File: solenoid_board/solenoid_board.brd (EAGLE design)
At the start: 30.1 x 30.1 mm, 19 parts, among them Q1 MOSFET-NCHANNELSMD, Q2 MOSFET-NCHANNELSMD, Q3 MOSFET-NCHANNELSMD, Q4 MOSFET-NCHANNELSMD

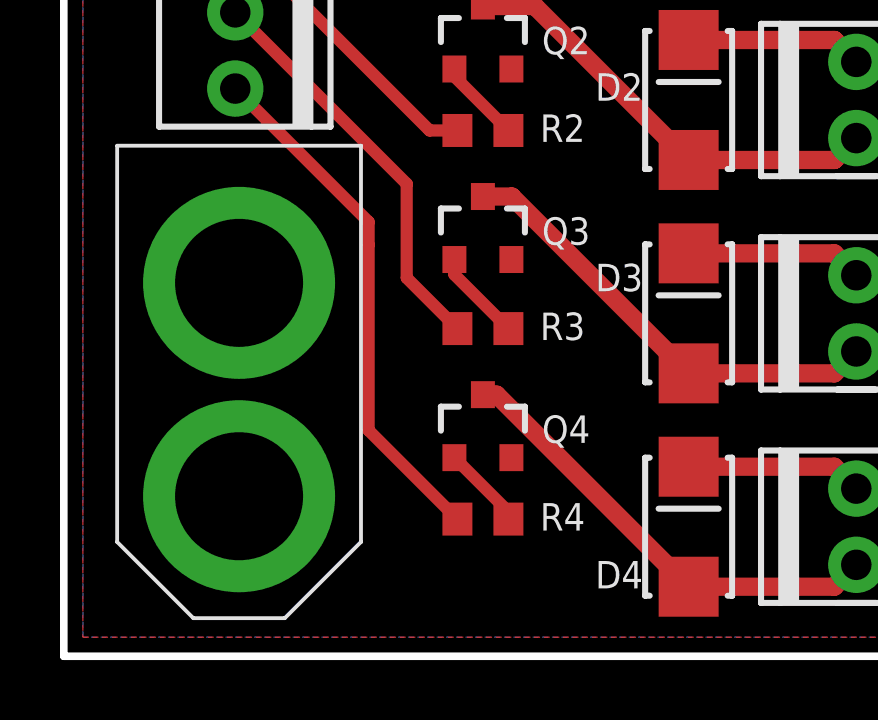
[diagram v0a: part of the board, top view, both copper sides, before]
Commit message: Fixed XT60 connector in pie.lbr. Changed battery connector on sherlock to have 4 pins instead of 5. Replaced XT60 on sherlock, solenoid board, and grizzly bear with new version.
Change-Id: Ic4b688068eb477e37db8d2c4f2efb7678e25c5b6
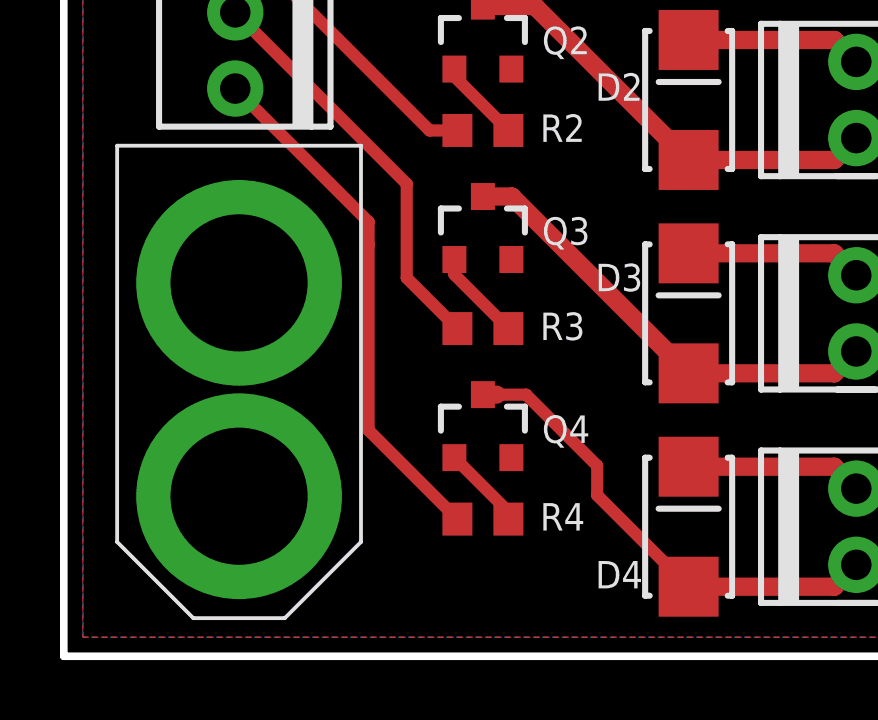
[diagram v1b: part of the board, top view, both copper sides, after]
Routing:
- net N$3: track 15.4 -> 16.0 mm
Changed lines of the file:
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@@
 <?xml version="1.0" encoding="utf-8"?>
 <!DOCTYPE eagle SYSTEM "eagle.dtd">
-<eagle version="6.2">
+<eagle version="6.3">
 <drawing>
 <settings>
@@
 </class>
 </classes>
-<designrules>
+<designrules name="advancedcircuits-33each-pie">
 <description language="de">&lt;b&gt;EAGLE Design Rules&lt;/b&gt;
 &lt;p&gt;
@@
 <param name="mtIsolate" value="9mil 40mil 9mil 0.1499mm 0.2007mm 0.1499mm 0.2007mm 0.1499mm 0.2007mm 0.1499mm 0.2007mm 0.1499mm 0.2007mm 0.1499mm 0.2007mm"/>
 <param name="mdWireWire" value="6mil"/>
-<param name="mdWirePad" value="6mil"/>
+<param name="mdWirePad" value="10mil"/>
 <param name="mdWireVia" value="6mil"/>
 <param name="mdPadPad" value="6mil"/>
@@
 <param name="mdViaViaSameLayer" value="8mil"/>
 <param name="mnLayersViaInSmd" value="2"/>
-<param name="mdCopperDimension" value="10mil"/>
+<param name="mdCopperDimension" value="25mil"/>
 <param name="mdDrill" value="7mil"/>
 <param name="mdSmdStop" value="0mil"/>
@@
 <wire x1="25.686" y1="2.318" x2="26.416" y2="3.048" width="0.6096" layer="1"/>
 <wire x1="13.97" y1="8.72" x2="14.426" y2="8.72" width="0.6096" layer="1"/>
-<wire x1="14.426" y1="8.72" x2="20.828" y2="2.318" width="0.6096" layer="1"/>
+<wire x1="14.426" y1="8.72" x2="15.41" y2="8.72" width="0.4064" layer="1"/>
+<wire x1="15.41" y1="8.72" x2="17.78" y2="6.35" width="0.4064" layer="1"/>
+<wire x1="17.78" y1="6.35" x2="17.78" y2="5.366" width="0.4064" layer="1"/>
+<wire x1="17.78" y1="5.366" x2="20.828" y2="2.318" width="0.4064" layer="1"/>
 </signal>
 <signal name="N$4" class="1">

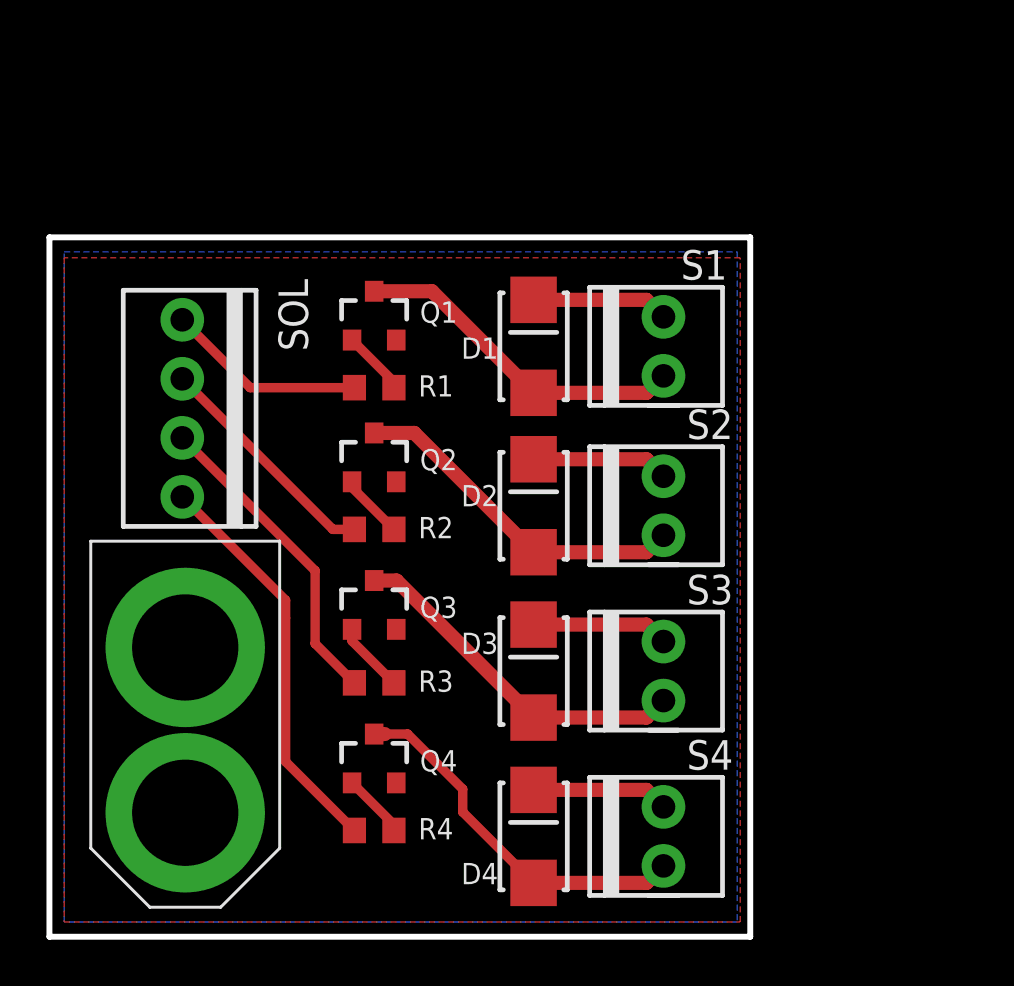
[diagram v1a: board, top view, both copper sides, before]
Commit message: Updated Solenoid Board to Rev C
- Added 10k pull-down resistors to MOSFET gates

DFM: https://www.freedfm.com/freedfm/0019486703400185/results/summary2.htm

Change-Id: I212b2e5e4622d924b76152e8610cd9dcc6a01ff7
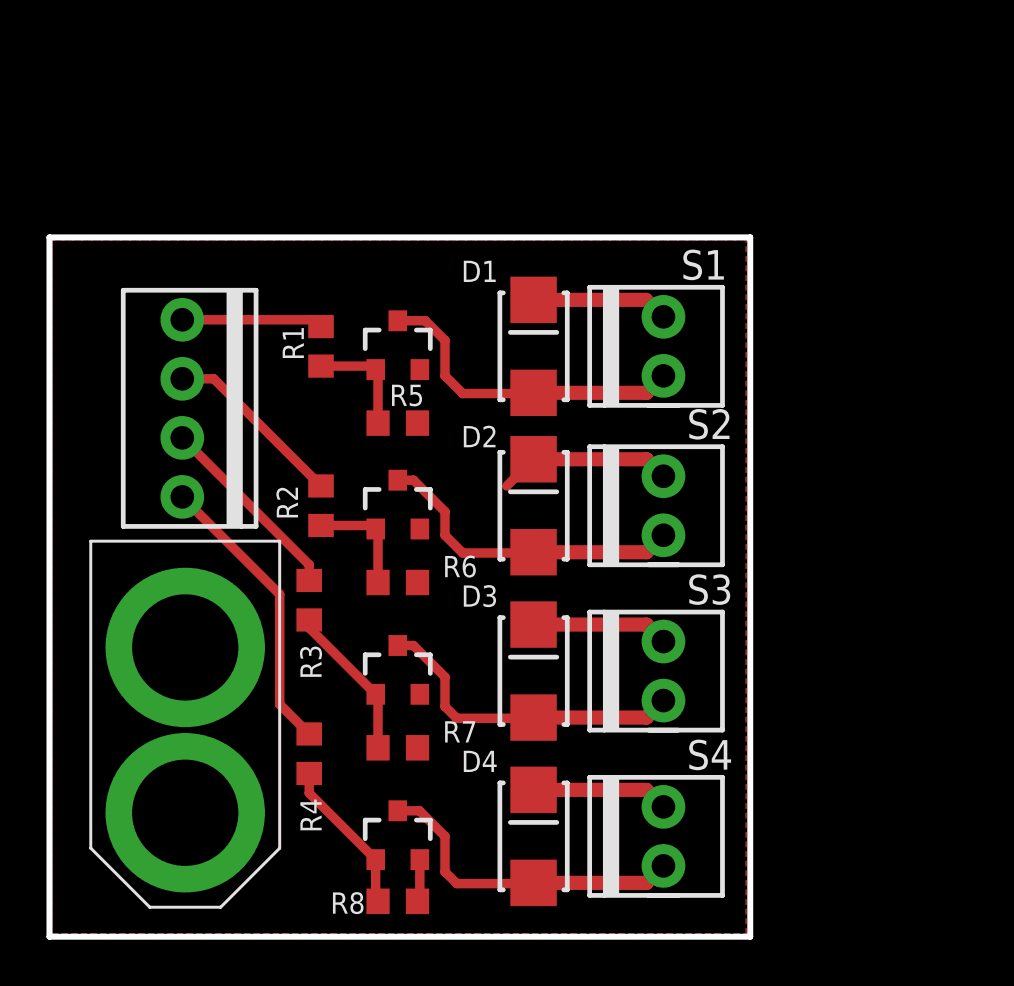
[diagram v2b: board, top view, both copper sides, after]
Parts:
- added R5, R6, R7, R8: 10k, resistor:R0603
- moved R3 4.52 mm to (11.2, 14.5), turned to 270 degrees
- moved R4 4.33 mm to (11.2, 7.87), turned to 270 degrees
- moved Q4 3.45 mm to (15.0, 4.32)
- moved Q3 2.97 mm to (15.0, 11.4)
- moved R1 2.90 mm to (11.7, 25.4), turned to 90 degrees
- moved R2 2.50 mm to (11.7, 18.5), turned to 270 degrees
- moved Q2 2.27 mm to (15.0, 18.5)
- moved Q1 1.63 mm to (15.0, 25.4)
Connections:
- net GND: now also R5.1, R6.1, R7.1, R8.1
- net N$15: now also R5.2
- net N$16: now also R6.2
- net N$17: now also R7.2
- net N$18: now also R8.2
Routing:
- net N$6: track 13.6 -> 8.40 mm
- net N$7: track 17.4 -> 12.5 mm
- net N$18: track 2.79 -> 6.78 mm
- net N$17: track 3.05 -> 6.78 mm
- net N$1: track 8.70 -> 6.09 mm
- net N$5: track 10.1 -> 7.88 mm
- net N$3: track 16.0 -> 13.9 mm
- net N$16: track 2.79 -> 4.82 mm
- net N$15: track 2.79 -> 4.82 mm
- net GND: track 0.05 -> 1.84 mm
- net 12V: track 23.6 -> 25.2 mm
- net N$4: track 15.2 -> 13.8 mm
- net N$8: track 14.9 -> 13.6 mm
- net N$2: track 14.6 -> 13.9 mm
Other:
- board text added: "2012.12.05"
- board text added: "Revision C"
- board text removed: "2012.11.19"
- board text removed: "Revision B"

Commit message: Updated Sherlock, Watson & Solenoid Board to Rev D. Updated pie.lbr.
- Put SSOP16 footprint and symbol (from Sparkfun.lbr) in pie.lbr.
  Can be used as a template for any SSOP16 device.
- Created SSOP14 footprint and symbol in pie.lbr using SSOP16.
  Can be used as a template for any SSOP14 device.
- Added QUADNOR device to pie.lbr
- Added VCC and enable pin to solenoid connector on Watson
- Added enable pin for solenoid board on Sherlock
- Added quad-NOR gate onto Solenoid Board
- Added VCC and enable pin for quad-NOR gate on Solenoid Board
- Added 0.1uF capacitors between VCC&GND and 12V&GND for Solenoid Board
- Added mounting holes to Solenoid Board
- Added additional holes to Sherlock and Watson for the testing jig
- Replaced all holes with standoff part in pie.lbr
- Gave each hole a value, either "Mounting", "Test" or "Mounting + Test"
  to state their purpose.
- Added/copied devices on boards that were NOT in pie.lbr TO pie.lbr
- Removed unnecessary packages from copied devices
- Manually set pad diameters for through-hole packages that were
  added/created/already there for these three boards
- Added PARTNUMBER attribute to the library parts added/copied/
  created/already there for these three boards
- Moved all Sherlock passives to the top

RYAN: I fixed what you asked for this revision. If this goes
through, I will then work on fixing everything else you told me to.

Sherlock DFM: https://www.freedfm.com/freedfm/0019486703414971/results/summary2.htm
Watson DFM: https://www.freedfm.com/freedfm/0019486703414975/results/summary2.htm
Solenoid Board DFM: https://www.freedfm.com/freedfm/0019486703414973/results/summary2.htm

Change-Id: Ie6b1bdecadde8b7bc780ad23041f2e110bf24a4c
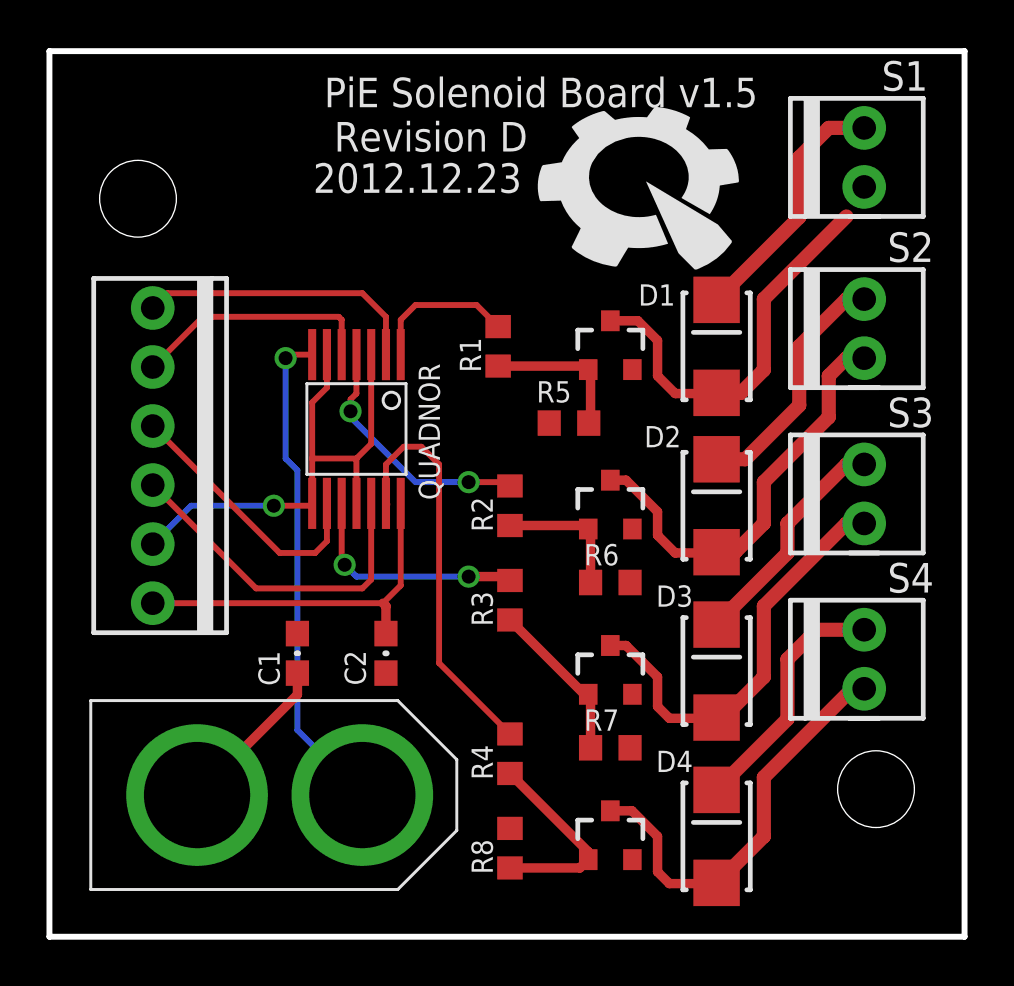
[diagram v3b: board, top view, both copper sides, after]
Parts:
- added C1, C2: 0.1uF, pie:0603-CAP
- added QUADNOR: SN74HC02DBR, pie:QUADNOR
- added U$3, U$4: Mounting + Test, pie:STAND-OFF
- D1, D2, D3, D4: device SparkFun:SMA-DIODE_ALT -> pie:SMA-DIODE_ALT
- Q1, Q2, Q3, Q4: device SparkFun:SOT23-3 -> pie:SOT23-3
- R1, R2, R3, R4, R5, R6, R7, R8: device resistor:R0603 -> pie:R0603
- S1, S2, S3, S4: device pie:1X02 -> pie:1X02-MTA
- SOL: device pie:1X04 -> pie:1X06-MTA
- moved U$1 17.5 mm to (25.7, 32.5), flipped to the top, turned to 0 degrees
- moved U$2 15.0 mm to (1.78, 2.03), turned to 0 degrees
- moved S1 11.9 mm to (35.1, 32.3)
- moved S2 11.5 mm to (35.1, 24.9)
- moved S3 11.5 mm to (35.1, 17.8)
- moved S4 11.5 mm to (35.1, 10.7)
- moved Q1 9.14 mm to (24.1, 25.4)
- moved Q2 9.14 mm to (24.1, 18.5)
- moved Q3 9.14 mm to (24.1, 11.4)
- moved Q4 9.14 mm to (24.1, 4.32)
- moved R6 9.14 mm to (24.1, 15.2)
- moved R7 9.14 mm to (24.1, 8.13)
- moved R3 8.64 mm to (19.8, 14.5)
- moved R4 8.64 mm to (19.8, 7.87)
- moved R2 8.13 mm to (19.8, 18.5)
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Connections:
- removed net N$1: R1.2, SOL.1
- removed net N$5: R2.1, SOL.2
- removed net N$6: R3.1, SOL.3
- removed net N$7: R4.1, SOL.4
- new net GATE1: QUADNOR.1Y, R1.2
- new net GATE2: QUADNOR.2Y, R2.1
- new net GATE3: QUADNOR.3Y, R3.1
- new net GATE4: QUADNOR.4Y, R4.1
- new net IO21: QUADNOR.3B, SOL.3
- new net IO61: QUADNOR.1B, QUADNOR.2B, QUADNOR.3A, QUADNOR.4A, SOL.5
- new net IO63: QUADNOR.2A, SOL.2
- new net IO64: QUADNOR.1A, SOL.1
- new net IO65: QUADNOR.4B, SOL.4
- new net VCC: C2.1, QUADNOR.VCC, SOL.6
- net 12V: now also C1.1
- net GND: now also C1.2, C2.2, QUADNOR.GND
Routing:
- net 12V: track 25.2 -> 49.3 mm
- net IO61: track 0.00 -> 22.8 mm, vias 0 -> 1
- net GND: track 1.84 -> 21.4 mm, vias 0 -> 1
- net GATE4: track 0.00 -> 17.5 mm
- net VCC: track 0.00 -> 15.9 mm
- net IO65: track 0.00 -> 14.7 mm
- net N$7: track 12.5 -> 0.00 mm
- net IO64: track 0.00 -> 12.3 mm
- net IO21: track 0.00 -> 11.6 mm
- net GATE2: track 0.00 -> 10.9 mm, vias 0 -> 2
- net IO63: track 0.00 -> 10.6 mm
- net GATE3: track 0.00 -> 10.1 mm, vias 0 -> 2
- net N$6: track 8.40 -> 0.00 mm
- net N$5: track 7.88 -> 0.00 mm
- net GATE1: track 0.00 -> 6.34 mm
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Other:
- board size 30.1 x 30.1 mm -> 39.4 x 38.1 mm
- board text added: "2012.12.23"
- board text added: "Revision D"
- board text removed: "2012.12.05"
- board text removed: "Revision C"
